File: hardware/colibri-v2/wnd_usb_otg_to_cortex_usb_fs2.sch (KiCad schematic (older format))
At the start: 14 parts

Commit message: Wired SDRAM pins. Added reset, power on/off for the WB module
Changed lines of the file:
@@
 $EndComp
 Wire Wire Line
-	4550 2250 4550 2600
-Wire Wire Line
-	4550 2600 4550 2800
+	4550 2250 4550 2800
 $Comp
 L +3V3 #PWR?
@@
 	6450 2200 6700 2200
 Wire Wire Line
-	6700 2050 6700 2200
-Wire Wire Line
-	6700 2200 6700 2600
+	6700 2050 6700 2600
 Wire Wire Line
 	6700 2600 6450 2600
@@
 	6500 4000 5200 4000
 Wire Wire Line
-	5200 3000 5200 4000
-Wire Wire Line
-	5200 4000 5200 4300
+	5200 3000 5200 4300
 Wire Wire Line
 	5200 3000 5350 3000
@@
 	7350 4700 6800 4700
 Wire Wire Line
-	6500 4300 5200 4300
-Wire Wire Line
-	5200 4300 4850 4300
+	4850 4300 6500 4300
 Text Notes 8800 4850 1    120  ~ 24
 DEVICE
@@
 	4550 4300 3250 4300
 Wire Wire Line
-	3250 4500 6000 4500
-Wire Wire Line
-	6000 4500 6500 4500
-Wire Wire Line
-	3250 4700 5600 4700
-Wire Wire Line
-	5600 4700 6500 4700
-$Comp
-L R_SMT R?
+	3250 4500 6500 4500
+Wire Wire Line
+	3250 4700 6500 4700
+$Comp
+L R_SMT R?

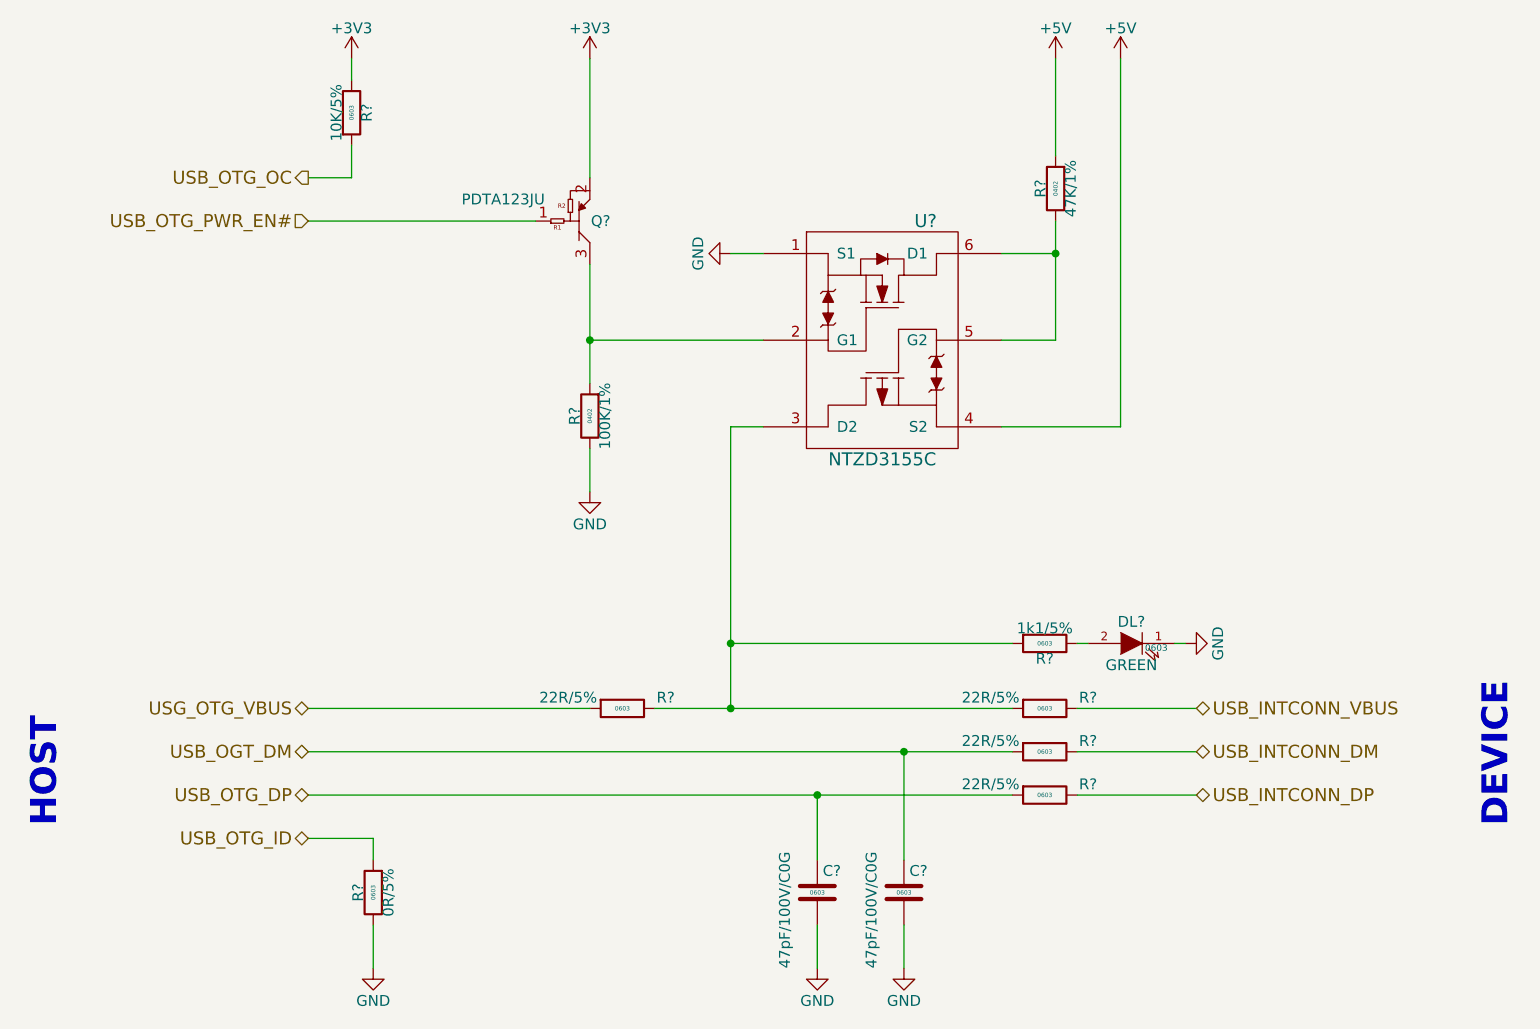
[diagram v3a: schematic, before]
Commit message: Resolving ERC problems
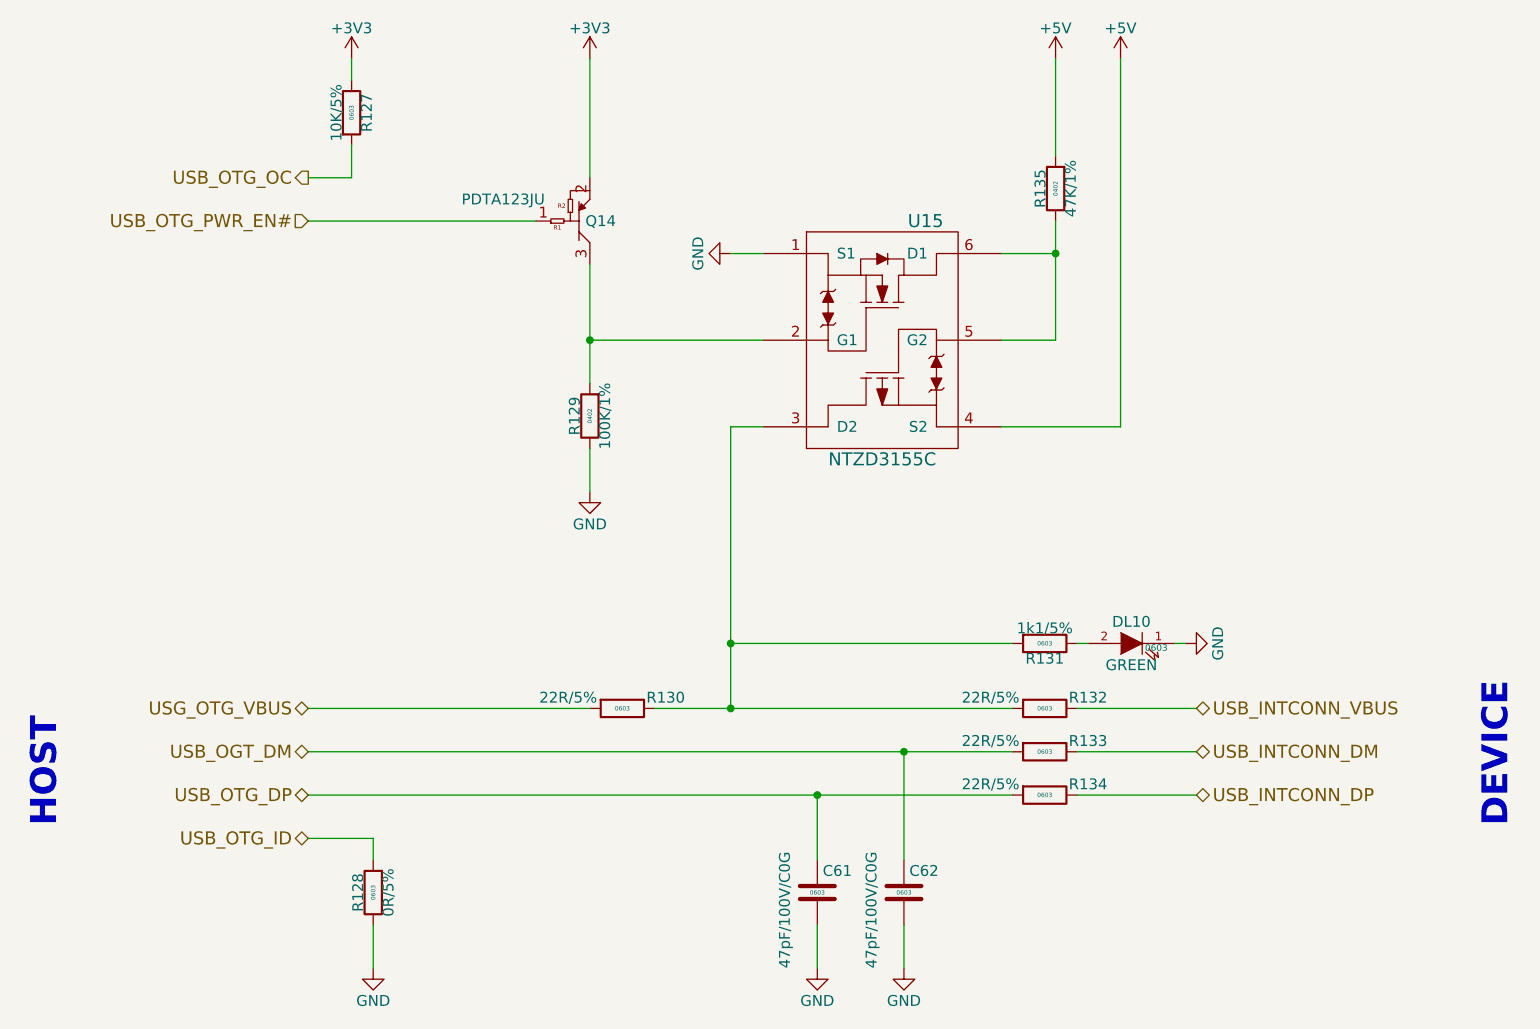
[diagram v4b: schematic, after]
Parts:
- gave numbers to parts that had none: 14
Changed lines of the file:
@@
 EESchema Schematic File Version 2
+LIBS:colibri-wnd-rescue
 LIBS:power
 LIBS:device
@@
 $EndDescr
 $Comp
-L RET_PNP_SMT Q?
+L RET_PNP_SMT Q14
 U 1 1 567A4E4B
 P 4500 2050
-F 0 "Q?" H 4600 2050 50  0000 C CNN
+F 0 "Q14" H 4600 2050 50  0000 C CNN
 F 1 "PDTA123JU" H 4150 1950 50  0000 C CNN
 F 2 "TO_SOT_Packages_SMD:SOT-323" H 4500 1760 30  0001 C CNN
@@
 $EndComp
 $Comp
-L R_SMT R?
+L R_SMT R129
 U 1 1 567A53B0
 P 4550 2950
-F 0 "R?" V 4620 2950 50  0000 C CNN
+F 0 "R129" V 4620 2950 50  0000 C CNN
 F 1 "100K/1%" V 4480 2950 50  0000 C CNN
 F 2 "Resistors_SMD:R_0402" V 4700 2950 30  0001 C CNN
@@
 $EndComp
 $Comp
-L NTZD3155C U?
+L NTZD3155C U15
 U 1 1 567A4FE9
 P 5900 2600
-F 0 "U?" H 6100 3150 60  0000 C CNN
+F 0 "U15" H 6100 3150 60  0000 C CNN
 F 1 "NTZD3155C" H 5900 2050 60  0000 C CNN
 F 2 "" H 5900 2600 60  0000 C CNN
@@
 $EndComp
 $Comp
-L GND #PWR?
+L GND #PWR0172
 U 1 1 567A50C7
 P 5200 2200
-F 0 "#PWR?" H 5200 1950 50  0001 C CNN
+F 0 "#PWR0172" H 5200 1950 50  0001 C CNN
 F 1 "GND" H 5200 2050 50  0000 C CNN
 F 2 "" H 5200 2200 50  0000 C CNN
@@
 	4550 2250 4550 2800
 $Comp
-L +3V3 #PWR?
+L +3V3 #PWR0173
 U 1 1 567A7B8E
 P 4550 1300
-F 0 "#PWR?" H 4550 1150 50  0001 C CNN
+F 0 "#PWR0173" H 4550 1150 50  0001 C CNN
 F 1 "+3V3" H 4550 1440 50  0000 C CNN
 F 2 "" H 4550 1300 50  0000 C CNN
@@
 	4550 2600 5350 2600
 $Comp
-L GND #PWR?
+L GND #PWR0174
 U 1 1 567A7E88
 P 4550 3300
-F 0 "#PWR?" H 4550 3050 50  0001 C CNN
+F 0 "#PWR0174" H 4550 3050 50  0001 C CNN
 F 1 "GND" H 4550 3150 50  0000 C CNN
 F 2 "" H 4550 3300 50  0000 C CNN
@@
 	6700 2600 6450 2600
 $Comp
-L R_SMT R?
+L R_SMT R135
 U 1 1 567A87DD
 P 6700 1900
-F 0 "R?" V 6770 1900 50  0000 C CNN
+F 0 "R135" V 6770 1900 50  0000 C CNN
 F 1 "47K/1%" V 6630 1900 50  0000 C CNN
 F 2 "Resistors_SMD:R_0402" V 6850 1900 30  0001 C CNN
@@
 $EndComp
 $Comp
-L +5V #PWR?
+L +5V #PWR0175
 U 1 1 567A88AC
 P 6700 1300
-F 0 "#PWR?" H 6700 1150 50  0001 C CNN
+F 0 "#PWR0175" H 6700 1150 50  0001 C CNN
 F 1 "+5V" H 6700 1440 50  0000 C CNN
 F 2 "" H 6700 1300 50  0000 C CNN
@@
 Connection ~ 6700 2200
 $Comp
-L +5V #PWR?
+L +5V #PWR0176
 U 1 1 567A8908
 P 7000 1300
-F 0 "#PWR?" H 7000 1150 50  0001 C CNN
+F 0 "#PWR0176" H 7000 1150 50  0001 C CNN
 F 1 "+5V" H 7000 1440 50  0000 C CNN
 F 2 "" H 7000 1300 50  0000 C CNN
@@
 	7000 3000 6450 3000
 $Comp
-L R_SMT R?
+L R_SMT R133
 U 1 1 567AA0B8
 P 6650 4500
-F 0 "R?" V 6600 4700 50  0000 C CNN
+F 0 "R133" V 6600 4700 50  0000 C CNN
 F 1 "22R/5%" V 6600 4250 50  0000 C CNN
 F 2 "Resistors_SMD:R_0603" V 6800 4500 30  0001 C CNN
@@
 $EndComp
 $Comp
-L GND #PWR?
+L GND #PWR0177
 U 1 1 567AA0CD
 P 5600 5500
-F 0 "#PWR?" H 5600 5250 50  0001 C CNN
+F 0 "#PWR0177" H 5600 5250 50  0001 C CNN
 F 1 "GND" H 5600 5350 50  0000 C CNN
 F 2 "" H 5600 5500 60  0000 C CNN
@@
 $EndComp
 $Comp
-L C_SMT C?
+L C_SMT C61
 U 1 1 567AA0D6
 P 5600 5150
-F 0 "C?" H 5625 5250 50  0000 L CNN
+F 0 "C61" H 5625 5250 50  0000 L CNN
 F 1 "47pF/100V/C0G" V 5450 4800 50  0000 L CNN
 F 2 "Capacitors_SMD:C_0603" H 5630 5000 30  0001 L CNN
@@
 	5600 5500 5600 5300
 $Comp
-L GND #PWR?
+L GND #PWR0178
 U 1 1 567AA0DE
 P 6000 5500
-F 0 "#PWR?" H 6000 5250 50  0001 C CNN
+F 0 "#PWR0178" H 6000 5250 50  0001 C CNN
 F 1 "GND" H 6000 5350 50  0000 C CNN
 F 2 "" H 6000 5500 60  0000 C CNN
@@
 $EndComp
 $Comp
-L C_SMT C?
+L C_SMT C62
 U 1 1 567AA0E7
 P 6000 5150
-F 0 "C?" H 6025 5250 50  0000 L CNN
+F 0 "C62" H 6025 5250 50  0000 L CNN
 F 1 "47pF/100V/C0G" V 5850 4800 50  0000 L CNN
 F 2 "Capacitors_SMD:C_0603" H 6030 5000 30  0001 L CNN
@@
 	6000 5500 6000 5300
 $Comp
-L R_SMT R?
+L R_SMT R131
 U 1 1 567AAE2B
 P 6650 4000
-F 0 "R?" V 6720 4000 50  0000 C CNN
+F 0 "R131" V 6720 4000 50  0000 C CNN
 F 1 "1k1/5%" V 6580 4000 50  0000 C CNN
 F 2 "Resistors_SMD:R_0603" V 6800 4000 30  0001 C CNN
@@
 $EndComp
 $Comp
-L LED_SMT DL?
+L LED_SMT DL10
 U 1 1 567AAE35
 P 7050 4000
-F 0 "DL?" H 7050 4100 50  0000 C CNN
+F 0 "DL10" H 7050 4100 50  0000 C CNN
 F 1 "GREEN" H 7050 3900 50  0000 C CNN
 F 2 "LEDs:LED-0603" H 7050 3850 30  0001 C CNN
@@
 $EndComp
 $Comp
-L GND #PWR?
+L GND #PWR0179
 U 1 1 567AAE3C
 P 7300 4000
-F 0 "#PWR?" H 7300 3750 50  0001 C CNN
+F 0 "#PWR0179" H 7300 3750 50  0001 C CNN
 F 1 "GND" H 7300 3850 50  0000 C CNN
 F 2 "" H 7300 4000 60  0000 C CNN
@@
 USB_INTCONN_DP
 $Comp
-L R_SMT R?
+L R_SMT R134
 U 1 1 567ABE1C
 P 6650 4700
-F 0 "R?" V 6600 4900 50  0000 C CNN
+F 0 "R134" V 6600 4900 50  0000 C CNN
 F 1 "22R/5%" V 6600 4450 50  0000 C CNN
 F 2 "Resistors_SMD:R_0603" V 6800 4700 30  0001 C CNN
@@
 $EndComp
 $Comp
-L R_SMT R?
+L R_SMT R132
 U 1 1 567ABE57
 P 6650 4300
-F 0 "R?" V 6600 4500 50  0000 C CNN
+F 0 "R132" V 6600 4500 50  0000 C CNN
 F 1 "22R/5%" V 6600 4050 50  0000 C CNN
 F 2 "Resistors_SMD:R_0603" V 6800 4300 30  0001 C CNN
@@
 $EndComp
 $Comp
-L R_SMT R?
+L R_SMT R130
 U 1 1 567ABE95
 P 4700 4300
-F 0 "R?" V 4650 4500 50  0000 C CNN
+F 0 "R130" V 4650 4500 50  0000 C CNN
 F 1 "22R/5%" V 4650 4050 50  0000 C CNN
 F 2 "Resistors_SMD:R_0603" V 4850 4300 30  0001 C CNN
@@
 	3250 4700 6500 4700
 $Comp
-L R_SMT R?
+L R_SMT R128
 U 1 1 567AE976
 P 3550 5150
-F 0 "R?" V 3620 5150 50  0000 C CNN
+F 0 "R128" V 3620 5150 50  0000 C CNN
 F 1 "0R/5%" V 3480 5150 50  0000 C CNN
 F 2 "Resistors_SMD:R_0603" V 3700 5150 30  0001 C CNN
@@
 	3550 4900 3550 5000
 $Comp
-L GND #PWR?
+L GND #PWR0180
 U 1 1 567AEA7D
 P 3550 5500
-F 0 "#PWR?" H 3550 5250 50  0001 C CNN
+F 0 "#PWR0180" H 3550 5250 50  0001 C CNN
 F 1 "GND" H 3550 5350 50  0000 C CNN
 F 2 "" H 3550 5500 60  0000 C CNN
@@
 USB_OTG_OC
 $Comp
-L +3V3 #PWR?
+L +3V3 #PWR0181
 U 1 1 567B076B
 P 3450 1300
-F 0 "#PWR?" H 3450 1150 50  0001 C CNN
+F 0 "#PWR0181" H 3450 1150 50  0001 C CNN
 F 1 "+3V3" H 3450 1440 50  0000 C CNN
 F 2 "" H 3450 1300 60  0000 C CNN
@@
 	3450 1300 3450 1400
 $Comp
-L R_SMT R?
+L R_SMT R127
 U 1 1 567B0775
 P 3450 1550
-F 0 "R?" V 3520 1550 50  0000 C CNN
+F 0 "R127" V 3520 1550 50  0000 C CNN
 F 1 "10K/5%" V 3380 1550 50  0000 C CNN
 F 2 "Resistors_SMD:R_0603" V 3600 1550 30  0001 C CNN
